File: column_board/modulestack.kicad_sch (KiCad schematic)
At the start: 0 parts

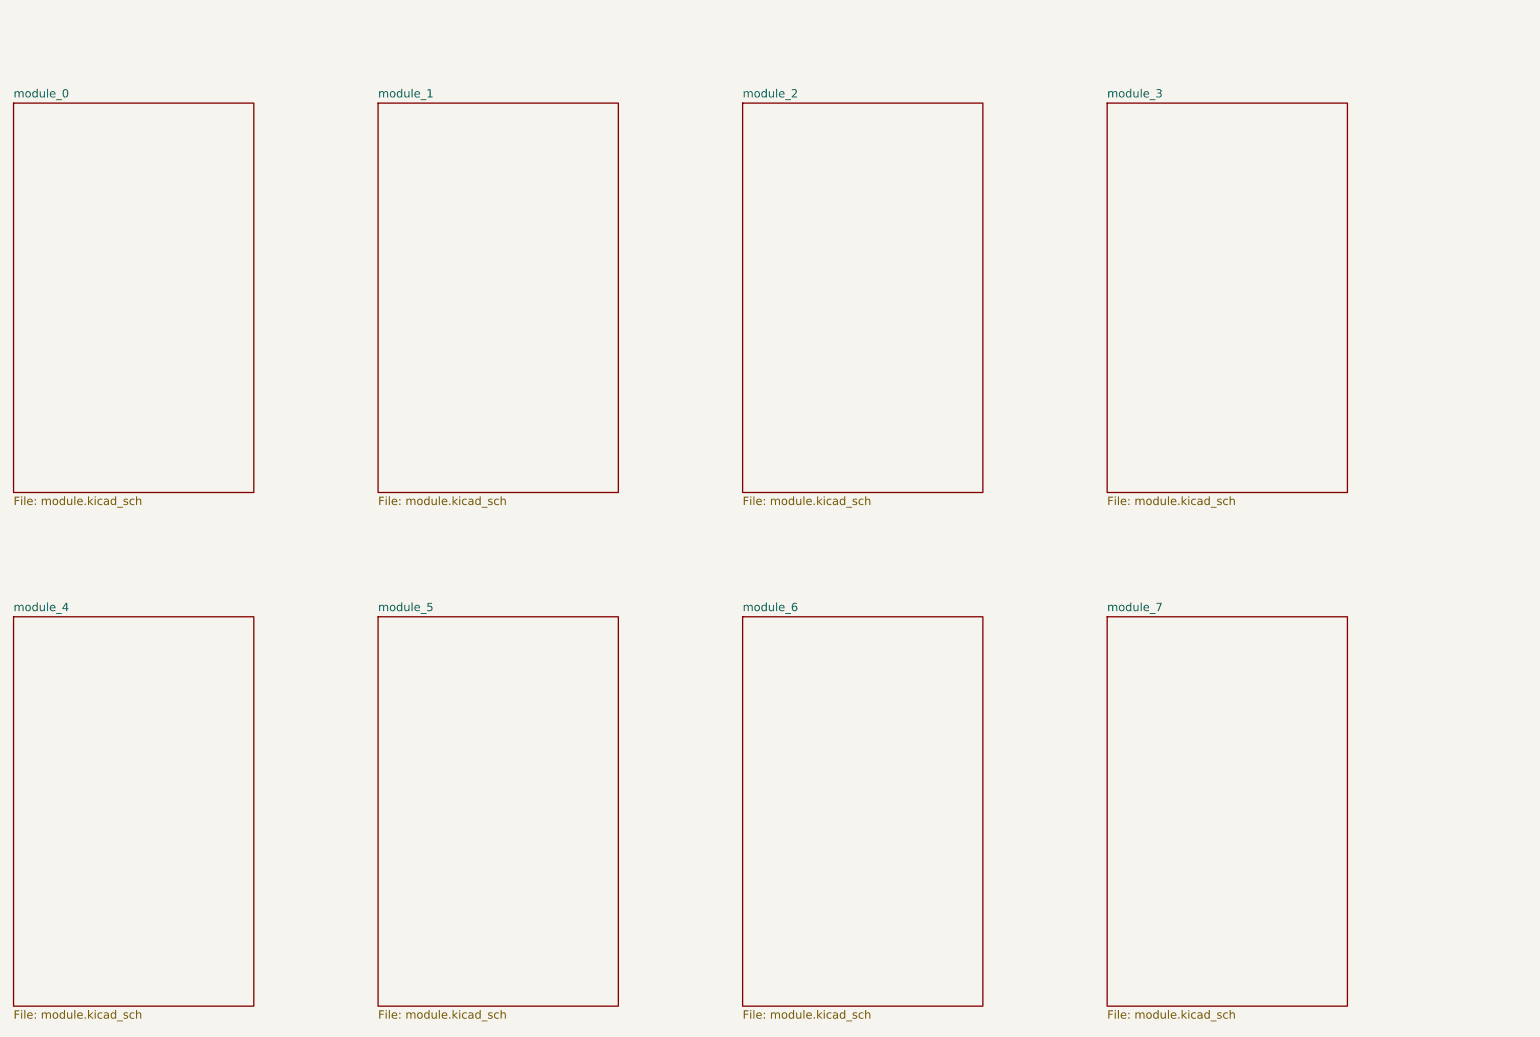
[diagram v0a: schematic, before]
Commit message: feat: create module connector system
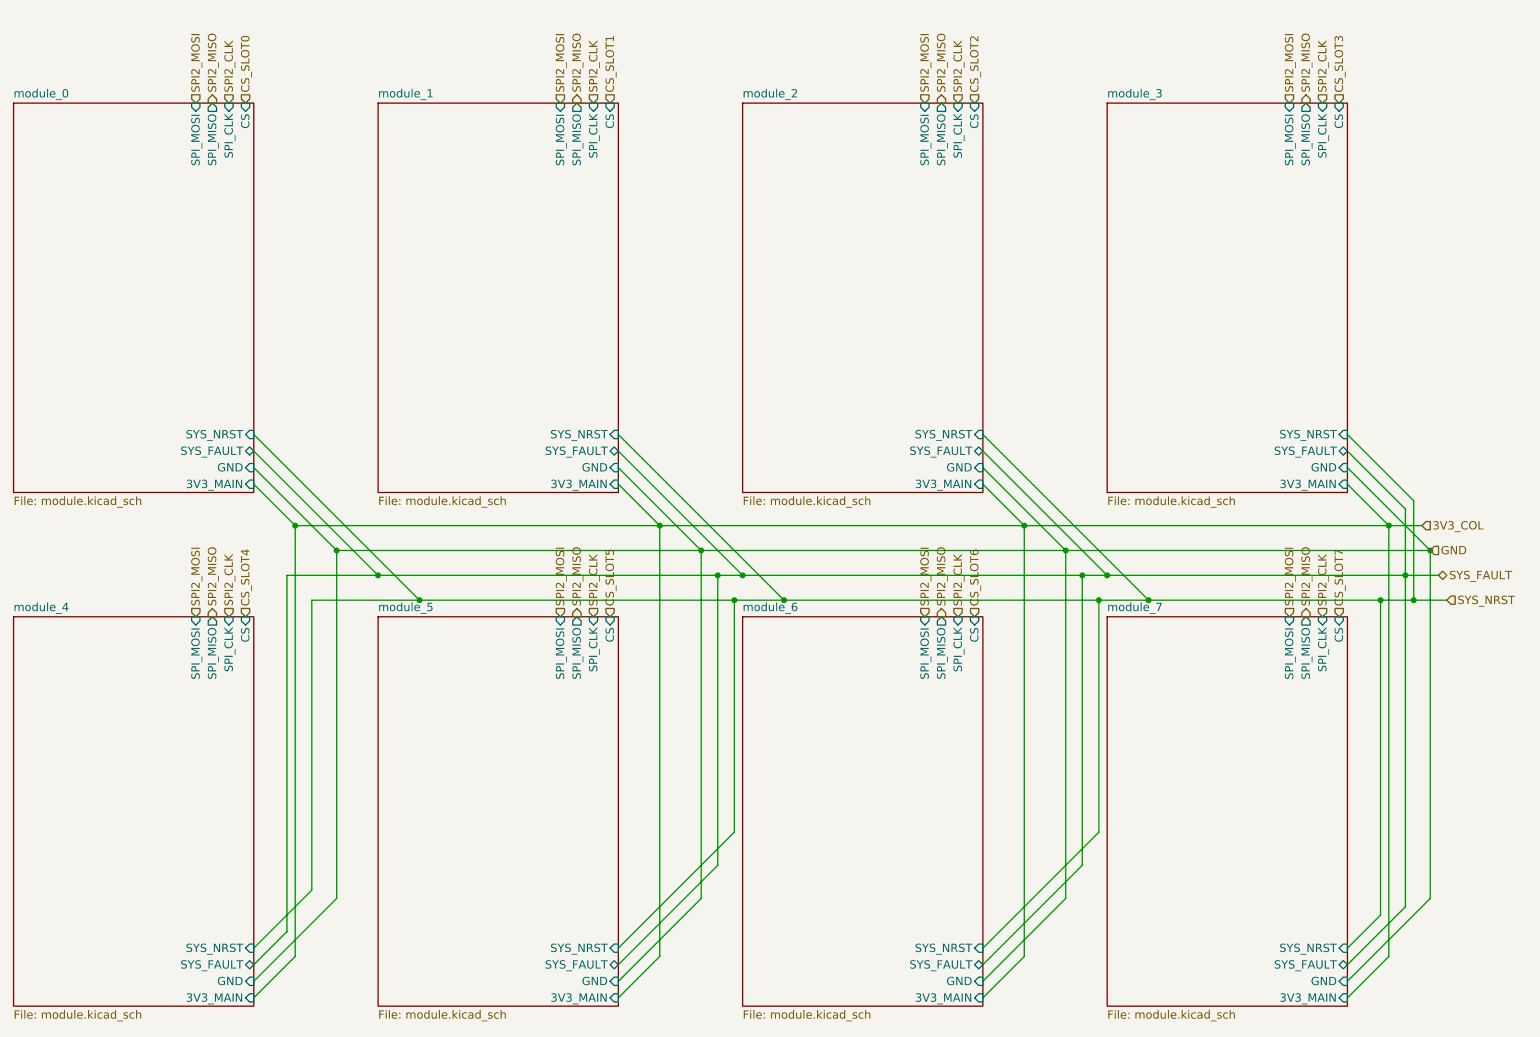
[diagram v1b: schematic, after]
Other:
- sheet module_0 ports: added 3V3_MAIN, CS, GND, SPI_CLK, SPI_MISO, SPI_MOSI, SYS_FAULT, SYS_NRST; removed none
- sheet module_1 ports: added 3V3_MAIN, CS, GND, SPI_CLK, SPI_MISO, SPI_MOSI, SYS_FAULT, SYS_NRST; removed none
- sheet module_2 ports: added 3V3_MAIN, CS, GND, SPI_CLK, SPI_MISO, SPI_MOSI, SYS_FAULT, SYS_NRST; removed none
- sheet module_3 ports: added 3V3_MAIN, CS, GND, SPI_CLK, SPI_MISO, SPI_MOSI, SYS_FAULT, SYS_NRST; removed none
- sheet module_4 ports: added 3V3_MAIN, CS, GND, SPI_CLK, SPI_MISO, SPI_MOSI, SYS_FAULT, SYS_NRST; removed none
- sheet module_5 ports: added 3V3_MAIN, CS, GND, SPI_CLK, SPI_MISO, SPI_MOSI, SYS_FAULT, SYS_NRST; removed none
- sheet module_6 ports: added 3V3_MAIN, CS, GND, SPI_CLK, SPI_MISO, SPI_MOSI, SYS_FAULT, SYS_NRST; removed none
- sheet module_7 ports: added 3V3_MAIN, CS, GND, SPI_CLK, SPI_MISO, SPI_MOSI, SYS_FAULT, SYS_NRST; removed none
